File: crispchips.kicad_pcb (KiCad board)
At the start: 2 copper layers, 113 parts, among them IC1 ISL85003FRZ, IC2 ISL9307IRTAANFZ-T7A, IC3 ESP32-S2-MINI-1-N4R2, IC4 XC3S250E-4VQG100C, IC5 PCA9306DCUR, IC6 W25N512GVEIG, J2 Conn_01x02_Male, J3 Conn_01x04, J4 JTAG, J5 HDMI_A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

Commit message: added gnd planes
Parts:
- moved C1 143.3 mm to (39.5, 87.7)
- moved IC2 143.3 mm to (54.8, 95.2)
- moved C10 143.3 mm to (61.4, 90.3)
- moved C11 143.3 mm to (61.4, 100.0)
- moved C2 143.3 mm to (42.7, 83.2)
- moved C3 143.3 mm to (41.2, 83.2)
- moved C4 143.3 mm to (49.2, 87.3)
- moved C5 143.3 mm to (47.7, 87.3)
- moved C6 143.3 mm to (50.7, 87.3)
- moved C7 143.3 mm to (55.8, 90.1)
- moved C8 143.3 mm to (56.1, 100.2)
- moved C9 143.3 mm to (51.0, 93.4)
- moved IC1 143.3 mm to (42.7, 87.3)
- moved J2 143.3 mm to (33.7, 82.0)
- moved L2 143.3 mm to (59.9, 93.6)
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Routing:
- net PG: track 25.7 -> 24.7 mm
- added copper zone on B.Cu, net GND
- added copper zone on F.Cu, net GND
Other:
- board outline added: 152.4 x 127 mm

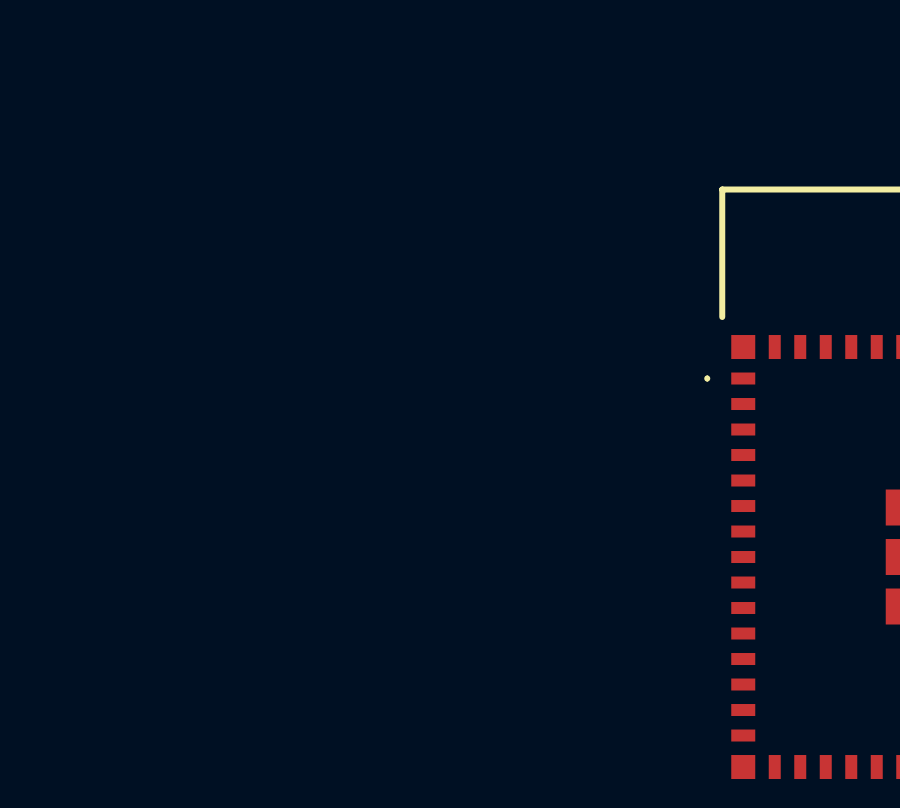
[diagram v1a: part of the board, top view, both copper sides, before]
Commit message: update footprint of jack
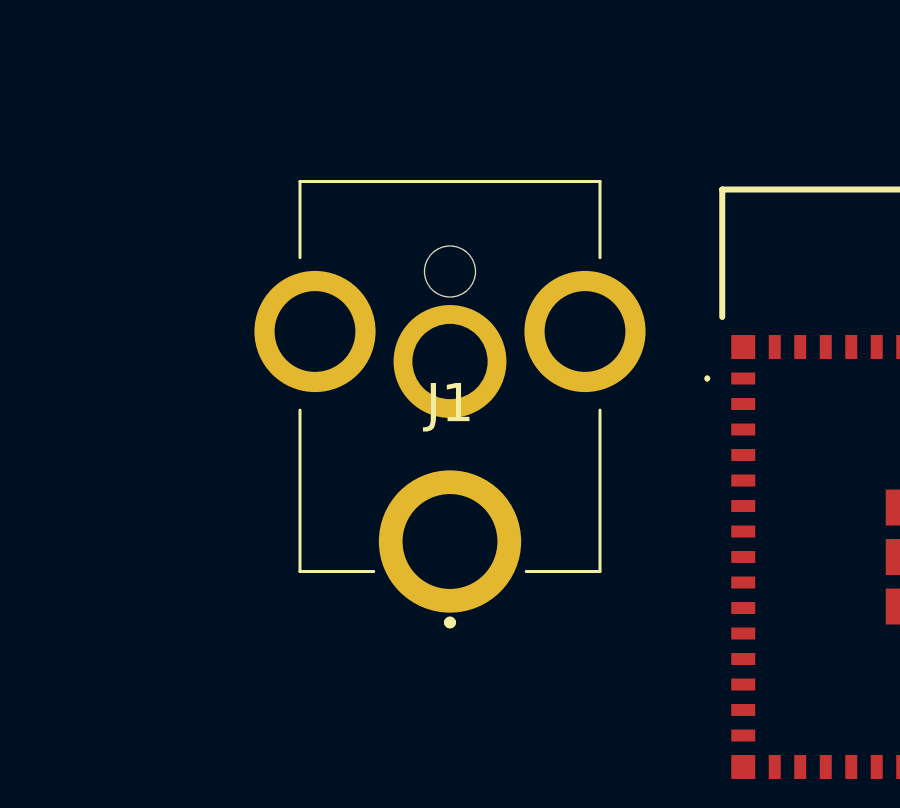
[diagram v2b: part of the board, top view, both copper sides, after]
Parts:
- added J1: Barrel_Jack, supply:PJ063BH, F.Cu at (101.1, 109.7)
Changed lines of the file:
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@@
     )
+  )
+  (footprint "supply:PJ063BH" (layer "F.Cu")
+    (at 101.092 109.728)
+    (descr "PJ-063BH")
+    (tags "Connector")
+    (property "Sheetfile" "supply.kicad_sch")
+    (property "Sheetname" "Supply")
+    (attr through_hole)
+    (fp_text reference "J1" (at 0 0) (layer "F.SilkS")
+      (effects (font (size 1.27 1.27) (thickness 0.254)))
+    )
+    (fp_text value "Barrel_Jack" (at 0 0) (layer "F.SilkS") hide
+      (effects (font (size 1.27 1.27) (thickness 0.254)))
+    )
+    (fp_text user "${REFERENCE}" (at 0 0) (layer "F.Fab")
+      (effects (font (size 1.27 1.27) (thickness 0.254)))
+    )
+    (fp_line (start 0.1 7.3) (end 0.1 7.3) (layer "F.SilkS") (width 0.2))
+    (fp_line (start 5 0.22) (end 5 5.6) (layer "F.SilkS") (width 0.1))
+    (fp_line (start -5 5.6) (end -2.54 5.6) (layer "F.SilkS") (width 0.1))
+    (fp_line (start -5 0.22) (end -5 5.6) (layer "F.SilkS") (width 0.1))
+    (fp_line (start -5 -4.86) (end -5 -7.4) (layer "F.SilkS") (width 0.1))
+    (fp_line (start 5 -7.4) (end 5 -4.86) (layer "F.SilkS") (width 0.1))
+    (fp_line (start -5 -7.4) (end 5 -7.4) (layer "F.SilkS") (width 0.1))
+    (fp_line (start 5 5.6) (end 2.54 5.6) (layer "F.SilkS") (width 0.1))
+    (fp_line (start -0.1 7.3) (end -0.1 7.3) (layer "F.SilkS") (width 0.2))
+    (fp_arc (start 0.1 7.3) (mid 0 7.4) (end -0.1 7.3) (layer "F.SilkS") (width 0.2))
+    (fp_arc (start -0.1 7.3) (mid 0 7.2) (end 0.1 7.3) (layer "F.SilkS") (width 0.2))
+    (fp_line (start 7.519 8.4) (end -7.519 8.4) (layer "F.CrtYd") (width 0.1))
+    (fp_line (start -7.519 8.4) (end -7.519 -8.4) (layer "F.CrtYd") (width 0.1))
+    (fp_line (start -7.519 -8.4) (end 7.519 -8.4) (layer "F.CrtYd") (width 0.1))
+    (fp_line (start 7.519 -8.4) (end 7.519 8.4) (layer "F.CrtYd") (width 0.1))
+    (fp_line (start -5 5.6) (end -5 -7.4) (layer "F.Fab") (width 0.2))
+    (fp_line (start -5 -7.4) (end 5 -7.4) (layer "F.Fab") (width 0.2))
+    (fp_line (start 5 5.6) (end -5 5.6) (layer "F.Fab") (width 0.2))
+    (fp_line (start 5 -7.4) (end 5 5.6) (layer "F.Fab") (width 0.2))
+    (pad "" np_thru_hole circle (at 0 -4.4) (size 1.7 1.7) (drill 1.7) (layers *.Cu *.Mask))
+    (pad "1" thru_hole circle (at 0 4.6) (size 4.743 4.743) (drill 3.1623) (layers *.Cu *.Mask)
+      (net 28 "Net-(IC1-Pad10)") (pintype "passive"))
+    (pad "2" thru_hole circle (at 0 -1.4) (size 3.762 3.762) (drill 2.508) (layers *.Cu *.Mask)
+      (net 2 "GND") (pintype "passive"))
+    (pad "3" thru_hole circle (at -4.5 -2.4) (size 4.039 4.039) (drill 2.6926) (layers *.Cu *.Mask))
+    (pad "4" thru_hole circle (at 4.5 -2.4) (size 4.039 4.039) (drill 2.6926) (layers *.Cu *.Mask))
   )
   (footprint "Capacitor_SMD:C_0603_1608Metric_Pad1.08x0.95mm_HandSolder" (layer "F.Cu")
